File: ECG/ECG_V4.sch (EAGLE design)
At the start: 32 parts, among them U1 AD8232, U3 BGM111-VISUAL-A

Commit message: Added LED circuit
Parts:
- added D2: RED, SparkFun-LED:LED-RED0603
- added R39: 1k, SparkFun-Resistors:1K-1%
- added SJ1: LED DISABLE, SparkFun-Passives:SOLDERJUMPERTRACE
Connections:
- new net N$36: D2.A, R39.1
- new net N$37: D2.C, SJ1.2
- new net N$38: R39.2
- net GND: now also SJ1.1
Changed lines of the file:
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@@
 <part name="JP1" library="LilyPad-Wearables" deviceset="SEWTAP" device="2"/>
 <part name="JP2" library="LilyPad-Wearables" deviceset="SEWTAP" device="2"/>
+<part name="R39" library="SparkFun-Resistors" deviceset="1K-1%" device="" value="1k"/>
+<part name="D2" library="SparkFun-LED" deviceset="LED-RED" device="0603" value="RED"/>
+<part name="GND12" library="SparkFun-Aesthetics" deviceset="GND" device=""/>
+<part name="SJ1" library="SparkFun-Passives" deviceset="SOLDERJUMPER" device="TRACE" value="LED DISABLE"/>
 </parts>
 <sheets>
@@
 <instance part="JP1" gate="G$1" x="27.94" y="134.62" rot="R180"/>
 <instance part="JP2" gate="G$1" x="27.94" y="124.46" rot="R180"/>
+<instance part="R39" gate="G$1" x="53.34" y="63.5"/>
+<instance part="D2" gate="G$1" x="43.18" y="63.5" rot="R270"/>
+<instance part="GND12" gate="1" x="15.24" y="55.88"/>
+<instance part="SJ1" gate="1" x="22.86" y="63.5"/>
 </instances>
 <busses>
@@
 <wire x1="170.18" y1="-20.32" x2="187.96" y2="-20.32" width="0.1524" layer="91"/>
 </segment>
+<segment>
+<pinref part="SJ1" gate="1" pin="1"/>
+<pinref part="GND12" gate="1" pin="GND"/>
+<wire x1="15.24" y1="58.42" x2="15.24" y2="63.5" width="0.1524" layer="91"/>
+<wire x1="15.24" y1="63.5" x2="17.78" y2="63.5" width="0.1524" layer="91"/>
+</segment>
 </net>
 <net name="N$1" class="0">
@@
 <wire x1="104.14" y1="7.62" x2="104.14" y2="60.96" width="0.1524" layer="91"/>
 <junction x="104.14" y="60.96"/>
-</segment>
-</net>
+<label x="66.04" y="63.5" size="1.27" layer="95" xref="yes"/>
+</segment>
+</net>
+<net name="N$36" class="0">
+<segment>
+<pinref part="R39" gate="G$1" pin="1"/>
+<pinref part="D2" gate="G$1" pin="A"/>
+<wire x1="45.72" y1="63.5" x2="48.26" y2="63.5" width="0.1524" layer="91"/>
+</segment>
+</net>
+<net name="N$37" class="0">
+<segment>
+<pinref part="D2" gate="G$1" pin="C"/>
+<pinref part="SJ1" gate="1" pin="2"/>
+<wire x1="38.1" y1="63.5" x2="27.94" y2="63.5" width="0.1524" layer="91"/>
+</segment>
+</net>
+<net name="N$38" class="0">
+<segment>
+<pinref part="R39" gate="G$1" pin="2"/>
+<wire x1="66.04" y1="63.5" x2="58.42" y2="63.5" width="0.1524" layer="91"/>
+</segment>
+</net>

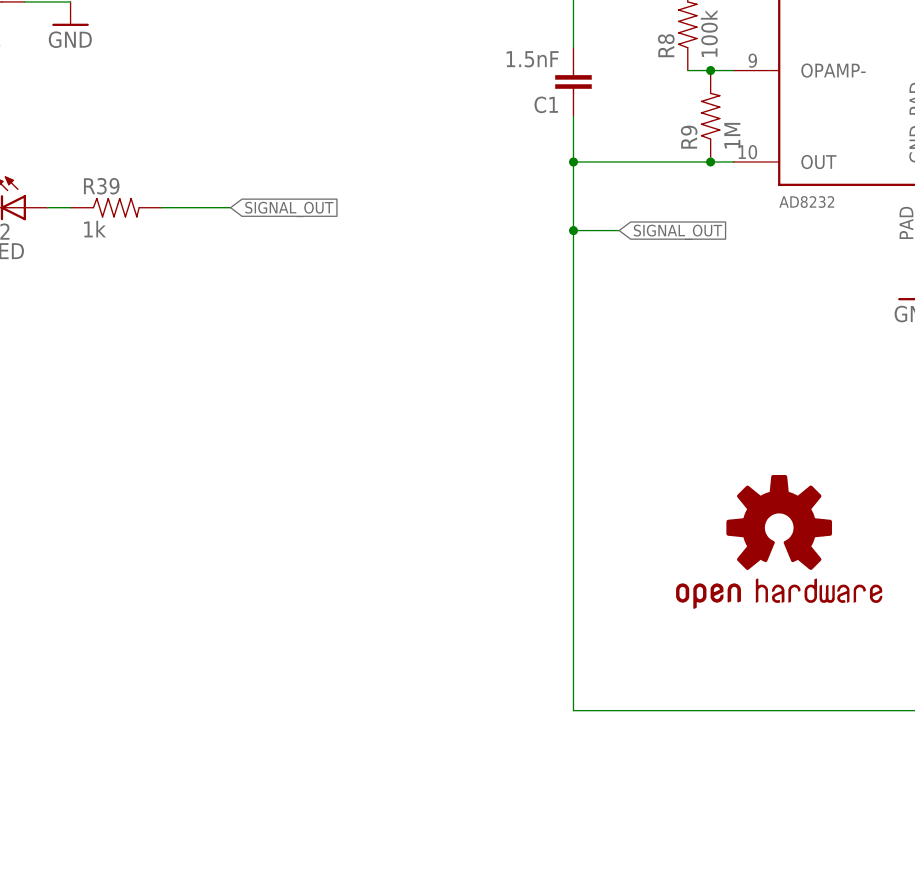
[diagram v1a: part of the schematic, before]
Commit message: Connections Debugged
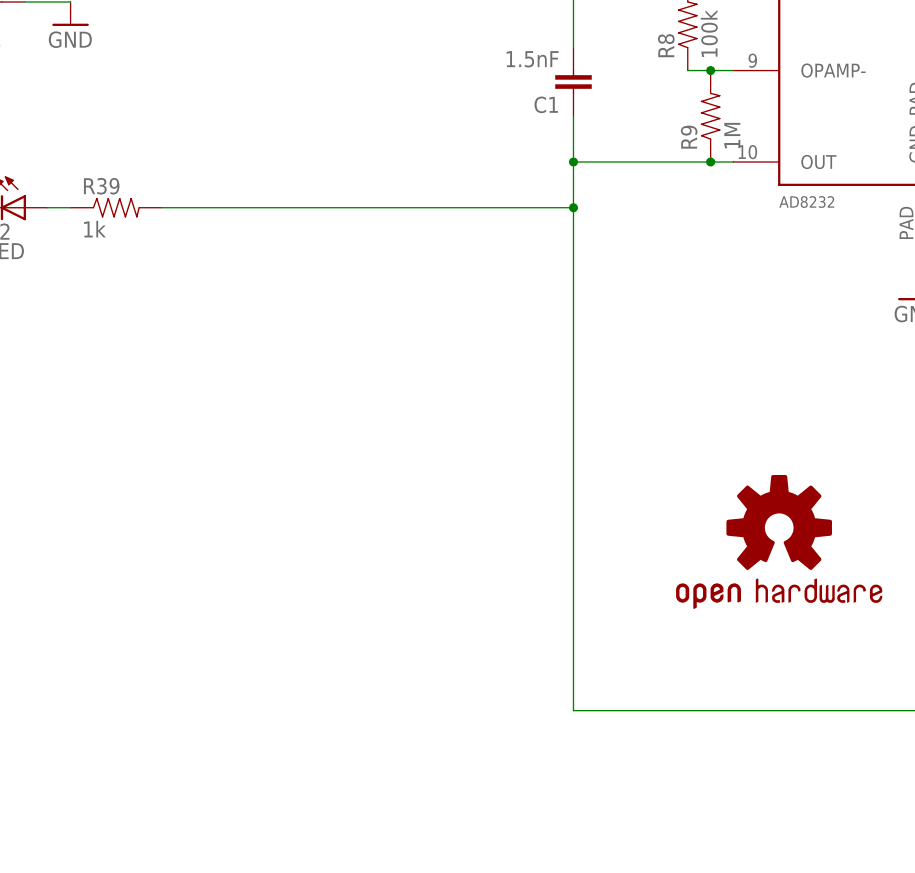
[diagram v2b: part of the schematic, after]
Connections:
- removed net N$38: R39.2
- net SIGNAL_OUT: now also R39.2
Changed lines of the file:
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@@
 <wire x1="104.14" y1="68.58" x2="104.14" y2="73.66" width="0.1524" layer="91"/>
 <junction x="119.38" y="68.58"/>
-<wire x1="104.14" y1="68.58" x2="104.14" y2="60.96" width="0.1524" layer="91"/>
-<wire x1="104.14" y1="60.96" x2="109.22" y2="60.96" width="0.1524" layer="91"/>
-<label x="109.22" y="60.96" size="1.27" layer="95" xref="yes"/>
 <junction x="104.14" y="68.58"/>
-<wire x1="104.14" y1="7.62" x2="104.14" y2="60.96" width="0.1524" layer="91"/>
-<junction x="104.14" y="60.96"/>
-<label x="66.04" y="63.5" size="1.27" layer="95" xref="yes"/>
+<wire x1="104.14" y1="7.62" x2="104.14" y2="63.5" width="0.1524" layer="91"/>
+<pinref part="R39" gate="G$1" pin="2"/>
+<wire x1="104.14" y1="63.5" x2="104.14" y2="68.58" width="0.1524" layer="91"/>
+<wire x1="58.42" y1="63.5" x2="104.14" y2="63.5" width="0.1524" layer="91"/>
+<junction x="104.14" y="63.5"/>
 </segment>
 </net>
@@
 </segment>
 </net>
-<net name="N$38" class="0">
-<segment>
-<pinref part="R39" gate="G$1" pin="2"/>
-<wire x1="66.04" y1="63.5" x2="58.42" y2="63.5" width="0.1524" layer="91"/>
-</segment>
-</net>
